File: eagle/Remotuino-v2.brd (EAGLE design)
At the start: 55.9 x 38.1 mm, 41 parts, among them Q1 16MHz, Q2 BSS138, Q3 BSS138, U1 ATMEGA324P, U2 MIC5209-3.3YS, U3 XBEE

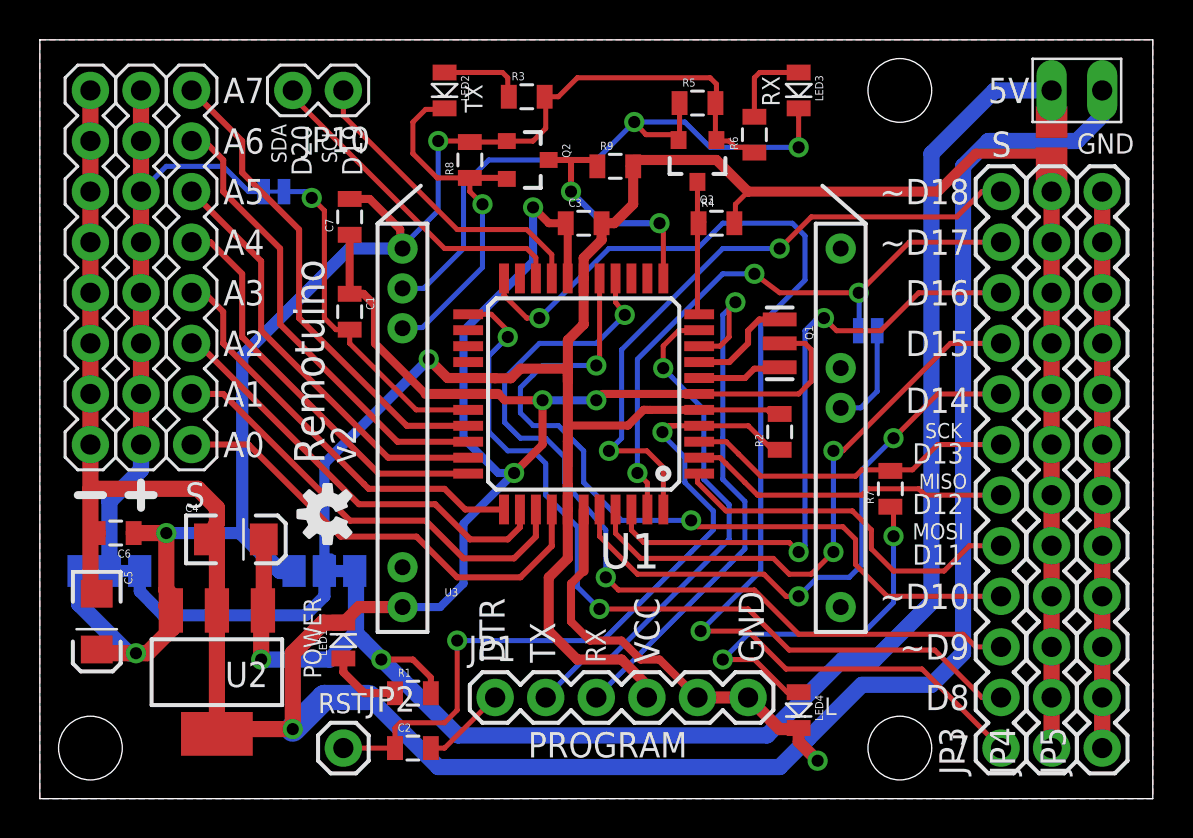
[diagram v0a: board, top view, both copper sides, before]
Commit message: 
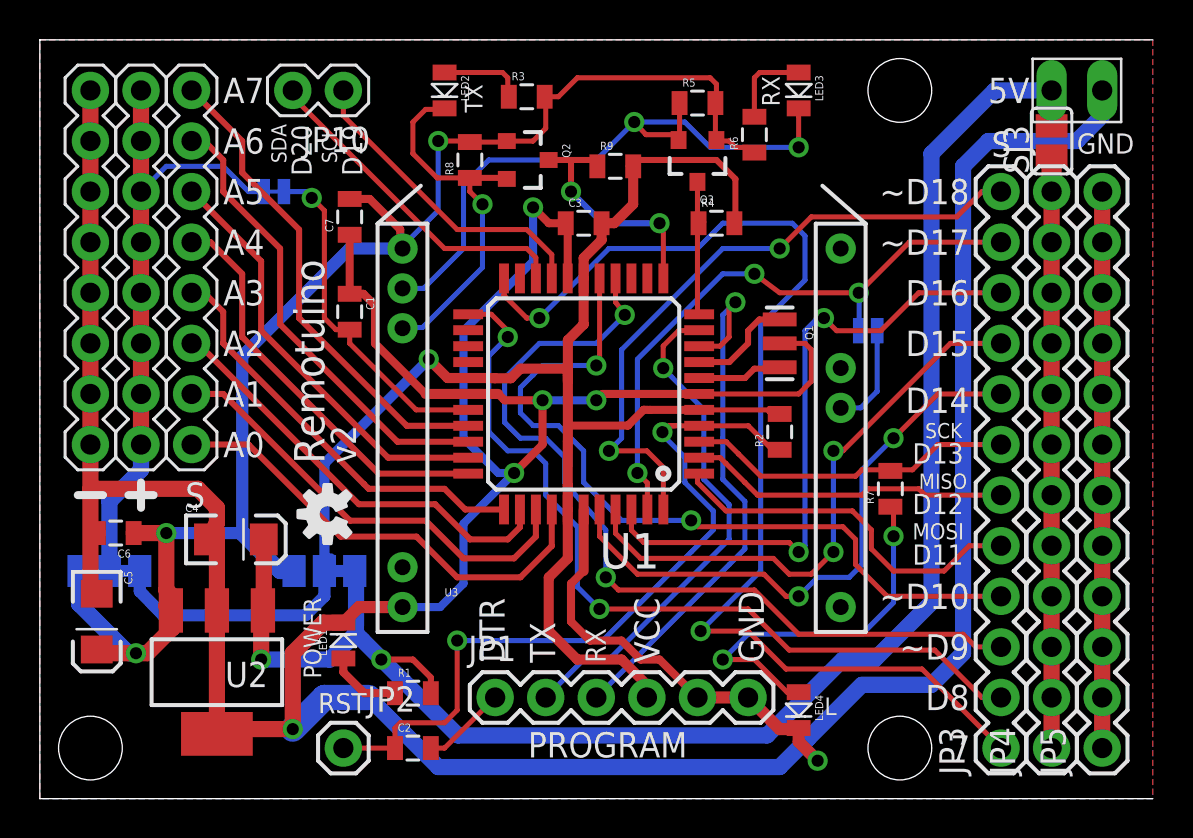
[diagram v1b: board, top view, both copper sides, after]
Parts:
- added SJ3: (no value), wibauxl:SJ
- JP4: value M12 -> (none)
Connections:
- new net V+: JP4.1, JP4.10, JP4.11, JP4.12, JP4.2, JP4.3, JP4.4, JP4.5, JP4.6, JP4.7, JP4.8, JP4.9, SJ3.1
- net VCC: no longer JP4.1, JP4.10, JP4.11, JP4.12, JP4.2, JP4.3, JP4.4, JP4.5, JP4.6, JP4.7, JP4.8, JP4.9
- net VIN: now also SJ3.2
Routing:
- net VCC: track 133.6 -> 88.4 mm
- net V+: track 0.00 -> 29.7 mm
- net VIN: track 84.9 -> 86.7 mm
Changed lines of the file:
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@@
 <setting verticaltext="up"/>
 </settings>
-<grid distance="0.0125" unitdist="inch" unit="mm" style="lines" multiple="8" display="yes" altdistance="6.25" altunitdist="mil" altunit="mil"/>
+<grid distance="0.0125" unitdist="inch" unit="mil" style="lines" multiple="8" display="yes" altdistance="6.25" altunitdist="mil" altunit="mil"/>
 <layers>
 <layer number="1" name="Top" color="4" fill="1" visible="yes" active="yes"/>
@@
 <layer number="220" name="220bmp" color="21" fill="1" visible="no" active="no"/>
 <layer number="221" name="221bmp" color="22" fill="1" visible="no" active="no"/>
+<layer number="222" name="222bmp" color="23" fill="1" visible="no" active="no"/>
 <layer number="223" name="223bmp" color="24" fill="1" visible="no" active="no"/>
 <layer number="224" name="224bmp" color="25" fill="1" visible="no" active="no"/>
@@
 <plain>
 <wire x1="0" y1="0" x2="55.88" y2="0" width="0" layer="20"/>
-<wire x1="55.88" y1="0" x2="55.88" y2="38.1" width="0" layer="20"/>
 <wire x1="55.88" y1="38.1" x2="0" y2="38.1" width="0" layer="20"/>
 <wire x1="0" y1="38.1" x2="0" y2="0" width="0" layer="20"/>
@@
 <text x="46.6724" y="5.715" size="1.27" layer="21" font="vector" ratio="15" rot="R180">D8</text>
 <text x="46.6725" y="31.1151" size="1.27" layer="21" font="vector" ratio="15" rot="R180">~D18</text>
-<rectangle x1="50.0063" y1="31.9088" x2="51.5938" y2="33.9725" layer="41"/>
-<rectangle x1="50.0063" y1="31.9088" x2="51.5937" y2="33.9724" layer="29"/>
 <hole x="43.18" y="35.56" drill="3.2"/>
 <hole x="2.54" y="2.54" drill="3.2"/>
 <hole x="43.18" y="2.54" drill="3.2"/>
-<rectangle x1="50.00625" y1="33.17875" x2="51.59375" y2="34.76625" layer="1"/>
-<rectangle x1="50.00625" y1="30.48" x2="51.59375" y2="32.7025" layer="1"/>
 </plain>
 <attributes>
@@
 <element name="U3" library="wibauxl" package="XBEE-MIN" value="XBEE" x="29.21" y="7.62"/>
 <element name="JP3" library="SparkFun" package="1X12" value="M12" x="48.26" y="2.54" rot="R90"/>
-<element name="JP4" library="SparkFun" package="1X12" value="M12" x="50.8" y="2.54" rot="R90"/>
+<element name="JP4" library="SparkFun" package="1X12" value="" x="50.8" y="2.54" rot="R90"/>
 <element name="JP5" library="SparkFun" package="1X12" value="M12" x="53.34" y="2.54" rot="R90"/>
 <element name="JP6" library="wibauxl" package="1X08" value="M8" x="7.62" y="17.78" rot="R90"/>
@@
 <element name="R9" library="SparkFun" package="0805" value="1K" x="28.8925" y="31.75"/>
 <element name="JP9" library="wibauxl" package="1X2_LONGPAD" value="" x="53.34" y="35.56"/>
+<element name="SJ3" library="wibauxl" package="SJ" value="" x="50.8" y="33.02" rot="R90"/>
 </elements>
 <signals>
@@
 <contactref element="C3" pad="2"/>
 <contactref element="R2" pad="2"/>
-<contactref element="JP4" pad="1"/>
-<contactref element="JP4" pad="2"/>
-<contactref element="JP4" pad="3"/>
-<contactref element="JP4" pad="4"/>
-<contactref element="JP4" pad="5"/>
-<contactref element="JP4" pad="6"/>
-<contactref element="JP4" pad="7"/>
-<contactref element="JP4" pad="8"/>
-<contactref element="JP4" pad="9"/>
-<contactref element="JP4" pad="10"/>
-<contactref element="JP4" pad="11"/>
-<contactref element="JP4" pad="12"/>
 <contactref element="U1" pad="5"/>
 <contactref element="U1" pad="17"/>
@@
 <contactref element="JP1" pad="4"/>
 <contactref element="SJ2" pad="1"/>
-<wire x1="50.8" y1="30.48" x2="50.8" y2="27.94" width="0.8128" layer="1"/>
-<wire x1="50.8" y1="27.94" x2="50.8" y2="25.4" width="0.8128" layer="1"/>
-<wire x1="50.8" y1="25.4" x2="50.8" y2="22.86" width="0.8128" layer="1"/>
-<wire x1="50.8" y1="22.86" x2="50.8" y2="20.32" width="0.8128" layer="1"/>
-<wire x1="50.8" y1="20.32" x2="50.8" y2="17.78" width="0.8128" layer="1"/>
-<wire x1="50.8" y1="17.78" x2="50.8" y2="15.24" width="0.8128" layer="1"/>
-<wire x1="50.8" y1="15.24" x2="50.8" y2="12.7" width="0.8128" layer="1"/>
-<wire x1="50.8" y1="12.7" x2="50.8" y2="10.16" width="0.8128" layer="1"/>
-<wire x1="50.8" y1="10.16" x2="50.8" y2="7.62" width="0.8128" layer="1"/>
-<wire x1="50.8" y1="7.62" x2="50.8" y2="5.08" width="0.8128" layer="1"/>
-<wire x1="50.8" y1="5.08" x2="50.8" y2="2.54" width="0.8128" layer="1"/>
-<wire x1="50.8" y1="32.0675" x2="50.8" y2="30.48" width="0.508" layer="1"/>
 <wire x1="33.105" y1="19.52" x2="36.6775" y2="19.52" width="0.254" layer="1"/>
 <wire x1="36.6775" y1="19.52" x2="36.83" y2="19.3675" width="0.254" layer="1"/>
@@
 <wire x1="21.505" y1="21.12" x2="22.3775" y2="21.12" width="0.508" layer="1"/>
 <wire x1="26.5113" y1="20.1614" x2="26.5113" y2="17.9388" width="0.508" layer="1"/>
-<wire x1="33.9725" y1="32.0675" x2="35.56" y2="30.48" width="0.508" layer="1"/>
-<wire x1="35.56" y1="30.48" x2="45.085" y2="30.48" width="0.508" layer="1"/>
 <wire x1="22.3775" y1="21.12" x2="22.8537" y2="21.1075" width="0.508" layer="1"/>
 <wire x1="22.8537" y1="21.1075" x2="23.6475" y2="21.1075" width="0.508" layer="1"/>
@@
 <wire x1="29.5275" y1="18.7325" x2="30.3213" y2="19.5263" width="0.4064" layer="1"/>
 <wire x1="26.5113" y1="20.1614" x2="26.5112" y2="19.5263" width="0.4064" layer="1"/>
-<wire x1="45.085" y1="30.48" x2="46.99" y2="32.385" width="0.508" layer="1"/>
-<wire x1="46.99" y1="32.385" x2="50.4825" y2="32.385" width="0.508" layer="1"/>
 <wire x1="26.5112" y1="21.2724" x2="26.5113" y2="20.1614" width="0.508" layer="1"/>
 <wire x1="27.305" y1="23.8125" x2="27.305" y2="26.12" width="0.508" layer="1"/>
@@
 <wire x1="34.8725" y1="28.8925" x2="34.925" y2="28.8925" width="0.254" layer="1"/>
 <wire x1="34.925" y1="28.8925" x2="34.925" y2="29.845" width="0.254" layer="1"/>
-<wire x1="34.925" y1="29.845" x2="35.56" y2="30.48" width="0.254" layer="1"/>
 <wire x1="24.13" y1="21.59" x2="26.5112" y2="21.59" width="0.508" layer="1"/>
 <contactref element="R9" pad="2"/>
 <wire x1="29.7925" y1="31.75" x2="29.5275" y2="31.75" width="0.254" layer="1"/>
-<wire x1="33.9725" y1="32.0675" x2="29.7925" y2="32.0675" width="0.508" layer="1"/>
 <wire x1="29.7925" y1="32.0675" x2="29.7925" y2="31.75" width="0.508" layer="1"/>
 <wire x1="29.7925" y1="29.845" x2="29.7925" y2="31.75" width="0.508" layer="1"/>
 <wire x1="28.205" y1="28.8925" x2="28.84" y2="28.8925" width="0.508" layer="1"/>
 <wire x1="28.84" y1="28.8925" x2="29.7925" y2="29.845" width="0.508" layer="1"/>
-<wire x1="50.4825" y1="32.385" x2="50.8" y2="32.0675" width="0.508" layer="1"/>
+<wire x1="29.7925" y1="32.0675" x2="33.9725" y2="32.0675" width="0.3048" layer="1"/>
+<wire x1="33.9725" y1="32.0675" x2="34.925" y2="31.115" width="0.3048" layer="1"/>
+<wire x1="34.925" y1="31.115" x2="34.925" y2="28.945" width="0.3048" layer="1"/>
+<wire x1="34.925" y1="28.945" x2="34.8725" y2="28.8925" width="0.3048" layer="1"/>
 </signal>
 <signal name="VIN">
@@
 <contactref element="JP9" pad="2"/>
 <wire x1="47.9425" y1="35.56" x2="50.8" y2="35.56" width="0.8128" layer="16"/>
+<contactref element="SJ3" pad="2"/>
+<wire x1="50.8" y1="33.782" x2="50.8" y2="35.56" width="1.016" layer="1"/>
 </signal>
 <signal name="D11/MOSI">
@@
 <wire x1="35.8775" y1="36.195" x2="35.8775" y2="34.2375" width="0.254" layer="1"/>
 </signal>
+<signal name="V+" class="1">
+<contactref element="JP4" pad="1"/>
+<contactref element="JP4" pad="2"/>
+<contactref element="JP4" pad="3"/>
+<contactref element="JP4" pad="4"/>
+<contactref element="JP4" pad="5"/>
+<contactref element="JP4" pad="6"/>
+<contactref element="JP4" pad="7"/>
+<contactref element="JP4" pad="8"/>
+<contactref element="JP4" pad="9"/>
+<contactref element="JP4" pad="10"/>
+<contactref element="JP4" pad="11"/>
+<contactref element="JP4" pad="12"/>
+<wire x1="50.8" y1="30.48" x2="50.8" y2="27.94" width="0.8128" layer="1"/>
+<wire x1="50.8" y1="27.94" x2="50.8" y2="25.4" width="0.8128" layer="1"/>
+<wire x1="50.8" y1="25.4" x2="50.8" y2="22.86" width="0.8128" layer="1"/>
+<wire x1="50.8" y1="22.86" x2="50.8" y2="20.32" width="0.8128" layer="1"/>
+<wire x1="50.8" y1="20.32" x2="50.8" y2="17.78" width="0.8128" layer="1"/>
+<wire x1="50.8" y1="17.78" x2="50.8" y2="15.24" width="0.8128" layer="1"/>
+<wire x1="50.8" y1="15.24" x2="50.8" y2="12.7" width="0.8128" layer="1"/>
+<wire x1="50.8" y1="12.7" x2="50.8" y2="10.16" width="0.8128" layer="1"/>
+<wire x1="50.8" y1="10.16" x2="50.8" y2="7.62" width="0.8128" layer="1"/>
+<wire x1="50.8" y1="7.62" x2="50.8" y2="5.08" width="0.8128" layer="1"/>
+<wire x1="50.8" y1="5.08" x2="50.8" y2="2.54" width="0.8128" layer="1"/>
+<contactref element="SJ3" pad="1"/>
+<wire x1="50.8" y1="32.258" x2="50.8" y2="30.48" width="1.016" layer="1"/>
+</signal>
 </signals>
+<errors>
+</errors>
 </board>
 </drawing>
